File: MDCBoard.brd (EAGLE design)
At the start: 43.9 x 32.6 mm, 200 parts, among them J1 JUMPER-SOLDER, J10 MICROSD-SOCKET, J11 USB-C-RECEPTACLE-KOREANHRO, J2 JUMPER-SOLDER, J3 JUMPER-SOLDER, J4 JUMPER-SOLDER, J5 JST-SM02B-SRSS-TB, J6 JUMPER-SOLDER, J7 JUMPER-SOLDER, J8 JUMPER-SOLDER, Q1 PMOS-NEXPERIA-SOT1220, Q2 PMOS-NEXPERIA-SOT1220, Q3 PMOS-NEXPERIA-SOT1220, Q4 DIODESINC-DMG2305UX, Q5 DIODESINC-DMG2305UX, Q6 DIODESINC-DMG2305UX, Q7 DIODESINC-DMG2305UX, Q8 DIODESINC-DMG2305UX, U1 TI-TPS2116, U10 TI-TPS22919DCK, U11 TI-TPS22919DCK, U12 TI-TPS22919DCK, U13 TI-TPS22919DCK, U14 TI-MSP430FR2422IRHL, U16 TI-TXB0102, U17 PANASONIC-EKMB110711X, U18 LATTICE-ICE40HX4K-BG121, U19 WINBOND-W25Q40EW, U2 DIODESINC-AP7350, U20 NEXPERIA-74LVC1G98-OR-INV-INP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, U21 NEXPERIA-74LVC1G98-BUFFER, U22 ON-AR0330CS1C12SPKA0, U23 ALLIANCE-AS4C8M16MSA-6BIN, U24 STM-STM32F730, U25 DIODESINC-DT1446-04V-7, U26 NEXPERIA-74LVC1G98-INVERTER, U3 NEXPERIA-74LVC1G98-NOR, U4 MICROCHIP-MCP7383X, U5 NEXPERIA-74LVC1G98-INVERTER, U6 EATON-STN101, U7 TI-TPS62A01, U8 TI-TPS62A01, U9 TI-TPS62A01, X1 EPSON-FC-135, X2 SITIME-SIT8021, X3 SITIME-SIT8021

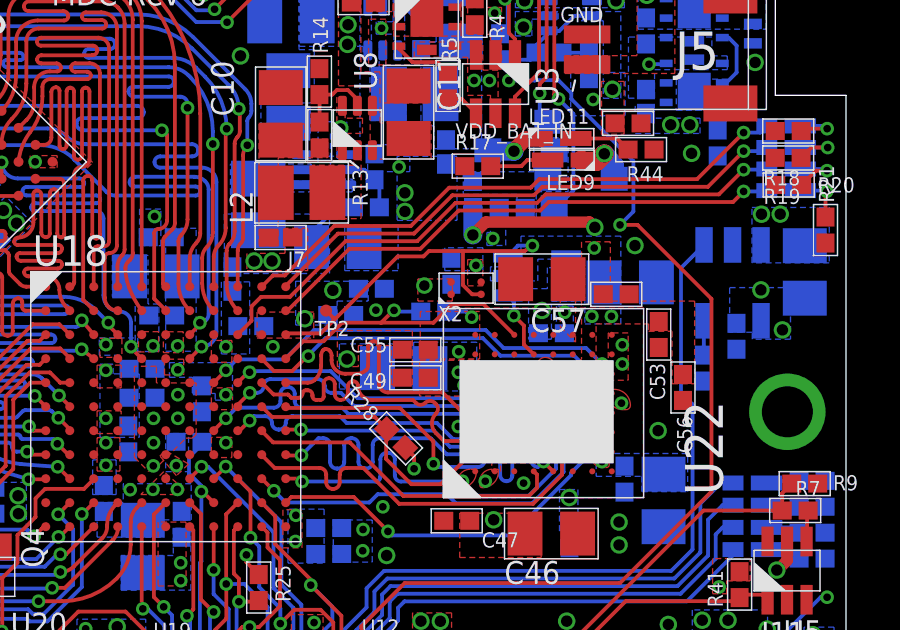
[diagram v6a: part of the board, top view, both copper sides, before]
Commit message: Move components further from lens mount ring
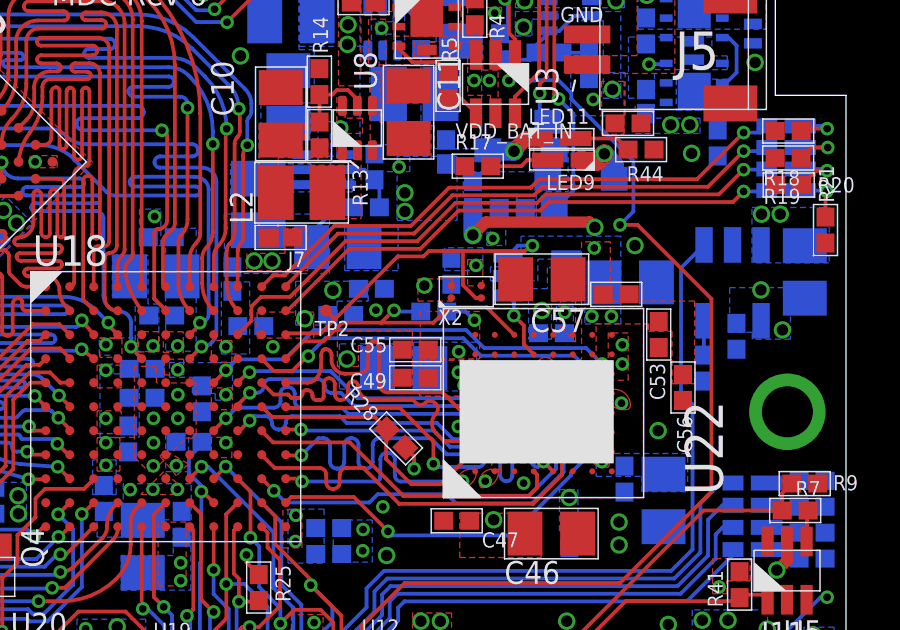
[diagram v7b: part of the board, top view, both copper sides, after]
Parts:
- moved X2 0.12 mm to (31.2, 21.4)
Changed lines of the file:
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@@
 <attribute name="PN" value="GRM155R61H104KE19D" x="37.613171875" y="19.968" size="1.778" layer="27" rot="R270" display="off"/>
 </element>
-<element name="X2" library="EagleLibrary" package="SITIME-SIT8021" value="SITIME-SIT8021" x="31.1912" y="21.513078125" smashed="yes" rot="R90" grouprefs="_ICE_IMG_CLK">
-<attribute name="MFG" value="SiTime" x="31.1912" y="21.513078125" size="1.778" layer="27" rot="R90" display="off"/>
-<attribute name="NAME" x="31.07961875" y="20.914496875" size="0.508" layer="25" font="vector" rot="R180"/>
-<attribute name="PN" value="SIT8021AI-J4-18S-16.000000E" x="31.1912" y="21.513078125" size="1.778" layer="27" rot="R90" display="off"/>
+<element name="X2" library="EagleLibrary" package="SITIME-SIT8021" value="SITIME-SIT8021" x="31.196278125" y="21.393696875" smashed="yes" rot="R90" grouprefs="_ICE_IMG_CLK">
+<attribute name="MFG" value="SiTime" x="31.196278125" y="21.393696875" size="1.778" layer="27" rot="R90" display="off"/>
+<attribute name="NAME" x="31.084696875" y="20.795115625" size="0.508" layer="25" font="vector" rot="R180"/>
+<attribute name="PN" value="SIT8021AI-J4-18S-16.000000E" x="31.196278125" y="21.393696875" size="1.778" layer="27" rot="R90" display="off"/>
 </element>
 <element name="J10" library="EagleLibrary" package="MOLEX-1051620001" value="MICROSD-SOCKET" x="8.78433125" y="8.73151875" smashed="yes" rot="MR180">
@@
 <wire x1="26.5237" y1="20.765559375" x2="26.775790625" y2="20.51346875" width="0.127" layer="1"/>
 <wire x1="26.775790625" y1="20.51346875" x2="26.775790625" y2="20.43620625" width="0.127" layer="1"/>
-<wire x1="31.6912" y1="21.308078125" x2="31.391840625" y2="21.308078125" width="0.127" layer="1"/>
-<wire x1="31.391840625" y1="21.308078125" x2="31.087059375" y2="21.612859375" width="0.127" layer="1"/>
+<wire x1="31.696278125" y1="21.188696875" x2="31.511221875" y2="21.188696875" width="0.127" layer="1"/>
+<wire x1="31.511221875" y1="21.188696875" x2="31.087059375" y2="21.612859375" width="0.127" layer="1"/>
 <via x="33.401" y="22.931121875" extent="1-16" drill="0.254"/>
 <wire x1="33.1409875" y1="22.75078125" x2="33.401" y2="22.931121875" width="0.127" layer="1"/>
@@
 <wire x1="25.9333" y1="19.24781875" x2="25.9333" y2="19.27609375" width="0.127" layer="16"/>
 <wire x1="26.502228125" y1="19.845021875" x2="25.9333" y2="19.27609375" width="0.127" layer="16"/>
-<wire x1="26.502228125" y1="19.845021875" x2="31.75" y2="19.845021875" width="0.127" layer="16"/>
+<wire x1="26.502228125" y1="19.845021875" x2="31.097221875" y2="19.845021875" width="0.127" layer="16"/>
 <wire x1="35.72246875" y1="18.332240625" x2="35.72245625" y2="18.33225625" width="0.127" layer="1"/>
 <wire x1="35.72245625" y1="18.33225625" x2="35.3972" y2="18.007" width="0.127" layer="1"/>
-<wire x1="31.75" y1="19.845021875" x2="32.333140625" y2="19.26188125" width="0.127" layer="16"/>
+<wire x1="31.097221875" y1="19.845021875" x2="31.6803625" y2="19.26188125" width="0.127" layer="16"/>
 <wire x1="34.792828125" y1="19.26188125" x2="35.72246875" y2="18.332240625" width="0.127" layer="16"/>
-<wire x1="32.333140625" y1="19.26188125" x2="34.792828125" y2="19.26188125" width="0.127" layer="16"/>
+<wire x1="31.6803625" y1="19.26188125" x2="34.792828125" y2="19.26188125" width="0.127" layer="16"/>
 </signal>
 <signal name="IMG_D2">
@@
 <wire x1="23.1836" y1="18.7672" x2="22.7794" y2="18.363" width="0.127" layer="1"/>
 <wire x1="25.14038125" y1="19.1389" x2="26.11934375" y2="20.1178625" width="0.127" layer="16"/>
-<wire x1="26.11934375" y1="20.1178625" x2="31.84144375" y2="20.1178625" width="0.127" layer="16"/>
+<wire x1="26.11934375" y1="20.1178625" x2="31.19628125" y2="20.1178625" width="0.127" layer="16"/>
 <wire x1="35.722471875" y1="18.985021875" x2="35.722471875" y2="18.982271875" width="0.127" layer="1"/>
 <wire x1="35.722471875" y1="18.982271875" x2="35.3972" y2="18.657" width="0.127" layer="1"/>
 <wire x1="23.1836" y1="18.7742" x2="23.5483" y2="19.1389" width="0.127" layer="16"/>
 <wire x1="23.5483" y1="19.1389" x2="25.14038125" y2="19.1389" width="0.127" layer="16"/>
-<wire x1="31.84144375" y1="20.1178625" x2="32.441946875" y2="19.517359375" width="0.127" layer="16"/>
+<wire x1="31.19628125" y1="20.1178625" x2="31.796784375" y2="19.517359375" width="0.127" layer="16"/>
 <wire x1="35.190134375" y1="19.517359375" x2="35.722471875" y2="18.985021875" width="0.127" layer="16"/>
-<wire x1="32.441946875" y1="19.517359375" x2="35.190134375" y2="19.517359375" width="0.127" layer="16"/>
+<wire x1="31.796784375" y1="19.517359375" x2="35.190134375" y2="19.517359375" width="0.127" layer="16"/>
 </signal>
 <signal name="VCCPLL0">
@@
 <wire x1="25.1794" y1="19.163" x2="25.75968125" y2="19.74328125" width="0.127" layer="1"/>
 <wire x1="25.75968125" y1="19.74328125" x2="26.44208125" y2="19.74328125" width="0.127" layer="1"/>
-<wire x1="30.103021875" y1="20.36064375" x2="30.722259375" y2="20.97988125" width="0.127" layer="1"/>
-<wire x1="31.77431875" y1="20.97988125" x2="30.722259375" y2="20.97988125" width="0.127" layer="1"/>
+<wire x1="30.103021875" y1="20.36064375" x2="30.61558125" y2="20.873203125" width="0.127" layer="1"/>
+<wire x1="31.880996875" y1="20.873203125" x2="30.61558125" y2="20.873203125" width="0.127" layer="1"/>
 <via x="28.788359375" y="20.77211875" extent="1-16" drill="0.254"/>
 <wire x1="28.7699375" y1="20.77211875" x2="28.788359375" y2="20.77211875" width="0.127" layer="1"/>
@@
 <wire x1="29.679728125" y1="20.732534375" x2="28.82794375" y2="20.732534375" width="0.127" layer="16"/>
 <wire x1="28.82794375" y1="20.732534375" x2="28.788359375" y2="20.77211875" width="0.127" layer="16"/>
-<wire x1="31.77431875" y1="20.97988125" x2="32.7972" y2="19.957" width="0.127" layer="1"/>
+<wire x1="31.880996875" y1="20.873203125" x2="32.7972" y2="19.957" width="0.127" layer="1"/>
 </signal>
 <signal name="IMG_SCLK">
@@
 <via x="4.364740625" y="4.99871875" extent="1-16" drill="0.254"/>
 <via x="4.364740625" y="4.295140625" extent="1-16" drill="0.254"/>
-<via x="31.377640625" y="20.546059375" extent="1-16" drill="0.254"/>
+<via x="31.4706" y="20.444459375" extent="1-16" drill="0.254"/>
 <via x="35.461971875" y="22.852384375" extent="1-16" drill="0.254"/>
 <via x="29.45714375" y="15.494" extent="1-16" drill="0.254"/>
@@
 <wire x1="4.673240625" y1="5.15570625" x2="4.673240625" y2="7.366" width="0.381" layer="15"/>
 <wire x1="4.673240625" y1="7.366" x2="4.673240625" y2="10.563953125" width="0.381" layer="15"/>
-<wire x1="30.544728125" y1="20.732534375" x2="31.191165625" y2="20.732534375" width="0.127" layer="16"/>
-<wire x1="31.191165625" y1="20.732534375" x2="31.377640625" y2="20.546059375" width="0.127" layer="16"/>
+<wire x1="30.544728125" y1="20.732534375" x2="31.16830625" y2="20.732534375" width="0.127" layer="16"/>
+<wire x1="31.16830625" y1="20.732534375" x2="31.4706" y2="20.444459375" width="0.127" layer="16"/>
 <via x="5.76071875" y="7.12978125" extent="1-16" drill="0.381"/>
 <wire x1="4.751525" y1="7.59434375" x2="5.2160875" y2="7.12978125" width="0.635" layer="1"/>
@@
 <wire x1="5.76071875" y1="7.12978125" x2="4.909459375" y2="7.12978125" width="0.381" layer="15"/>
 <wire x1="4.909459375" y1="7.12978125" x2="4.673240625" y2="7.366" width="0.381" layer="15"/>
-<wire x1="30.945840625" y1="19.395440625" x2="30.945840625" y2="20.114259375" width="0.381" layer="15"/>
-<wire x1="30.945840625" y1="20.114259375" x2="31.377640625" y2="20.546059375" width="0.381" layer="15"/>
-<wire x1="31.377640625" y1="20.546059375" x2="31.377640625" y2="20.555646875" width="0.381" layer="15"/>
-<wire x1="31.377640625" y1="20.555646875" x2="32.772146875" y2="21.950153125" width="0.381" layer="15"/>
+<wire x1="30.945840625" y1="19.395440625" x2="30.945840625" y2="19.93391875" width="0.381" layer="15"/>
+<wire x1="30.945840625" y1="19.93391875" x2="31.4706" y2="20.444459375" width="0.381" layer="15"/>
+<wire x1="31.4706" y1="20.444459375" x2="31.45638125" y2="20.6343875" width="0.381" layer="15"/>
+<wire x1="31.45638125" y1="20.6343875" x2="32.772146875" y2="21.950153125" width="0.381" layer="15"/>
 <wire x1="34.156978125" y1="22.852384375" x2="34.402784375" y2="22.852384375" width="0.381" layer="15"/>
 <wire x1="24.98630625" y1="25.654" x2="26.76430625" y2="27.432" width="0.381" layer="15"/>

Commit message: Layout progress
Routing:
- net GND: vias 77 -> 78
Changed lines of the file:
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@@
 <grid distance="10" unitdist="mil" unit="mil" style="lines" multiple="1" display="no" altdistance="0.00254" altunitdist="mm" altunit="mil"/>
 <layers>
-<layer number="1" name="Top" color="4" fill="1" visible="yes" active="yes"/>
+<layer number="1" name="Top" color="4" fill="1" visible="no" active="yes"/>
 <layer number="2" name="Ground" color="16" fill="1" visible="no" active="yes"/>
 <layer number="3" name="Route3" color="17" fill="1" visible="no" active="no"/>
@@
 <layer number="14" name="Route14" color="22" fill="1" visible="no" active="no"/>
 <layer number="15" name="Power" color="42" fill="1" visible="no" active="yes"/>
-<layer number="16" name="Bottom" color="1" fill="1" visible="no" active="yes"/>
+<layer number="16" name="Bottom" color="1" fill="1" visible="yes" active="yes"/>
 <layer number="17" name="Pads" color="2" fill="1" visible="yes" active="yes"/>
 <layer number="18" name="Vias" color="2" fill="1" visible="yes" active="yes"/>
 <layer number="19" name="Unrouted" color="6" fill="1" visible="no" active="yes"/>
 <layer number="20" name="Dimension" color="24" fill="1" visible="yes" active="yes"/>
-<layer number="21" name="tPlace" color="7" fill="1" visible="yes" active="yes"/>
-<layer number="22" name="bPlace" color="7" fill="1" visible="no" active="yes"/>
-<layer number="23" name="tOrigins" color="15" fill="1" visible="yes" active="yes"/>
-<layer number="24" name="bOrigins" color="15" fill="1" visible="no" active="yes"/>
-<layer number="25" name="tNames" color="7" fill="1" visible="yes" active="yes"/>
-<layer number="26" name="bNames" color="7" fill="1" visible="no" active="yes"/>
-<layer number="27" name="tValues" color="7" fill="1" visible="yes" active="yes"/>
-<layer number="28" name="bValues" color="7" fill="1" visible="no" active="yes"/>
-<layer number="29" name="tStop" color="7" fill="3" visible="yes" active="yes"/>
-<layer number="30" name="bStop" color="7" fill="6" visible="no" active="yes"/>
-<layer number="31" name="tCream" color="7" fill="4" visible="yes" active="yes"/>
-<layer number="32" name="bCream" color="7" fill="5" visible="no" active="yes"/>
-<layer number="33" name="tFinish" color="6" fill="3" visible="yes" active="yes"/>
-<layer number="34" name="bFinish" color="6" fill="6" visible="no" active="yes"/>
-<layer number="35" name="tGlue" color="7" fill="4" visible="yes" active="yes"/>
-<layer number="36" name="bGlue" color="7" fill="5" visible="no" active="yes"/>
-<layer number="37" name="tTest" color="7" fill="1" visible="yes" active="yes"/>
-<layer number="38" name="bTest" color="7" fill="1" visible="no" active="yes"/>
-<layer number="39" name="tKeepout" color="4" fill="11" visible="yes" active="yes"/>
-<layer number="40" name="bKeepout" color="1" fill="11" visible="no" active="yes"/>
-<layer number="41" name="tRestrict" color="4" fill="10" visible="yes" active="yes"/>
-<layer number="42" name="bRestrict" color="1" fill="10" visible="no" active="yes"/>
+<layer number="21" name="tPlace" color="7" fill="1" visible="no" active="yes"/>
+<layer number="22" name="bPlace" color="7" fill="1" visible="yes" active="yes"/>
+<layer number="23" name="tOrigins" color="15" fill="1" visible="no" active="yes"/>
+<layer number="24" name="bOrigins" color="15" fill="1" visible="yes" active="yes"/>
+<layer number="25" name="tNames" color="7" fill="1" visible="no" active="yes"/>
+<layer number="26" name="bNames" color="7" fill="1" visible="yes" active="yes"/>
+<layer number="27" name="tValues" color="7" fill="1" visible="no" active="yes"/>
+<layer number="28" name="bValues" color="7" fill="1" visible="yes" active="yes"/>
+<layer number="29" name="tStop" color="7" fill="3" visible="no" active="yes"/>
+<layer number="30" name="bStop" color="7" fill="6" visible="yes" active="yes"/>
+<layer number="31" name="tCream" color="7" fill="4" visible="no" active="yes"/>
+<layer number="32" name="bCream" color="7" fill="5" visible="yes" active="yes"/>
+<layer number="33" name="tFinish" color="6" fill="3" visible="no" active="yes"/>
+<layer number="34" name="bFinish" color="6" fill="6" visible="yes" active="yes"/>
+<layer number="35" name="tGlue" color="7" fill="4" visible="no" active="yes"/>
+<layer number="36" name="bGlue" color="7" fill="5" visible="yes" active="yes"/>
+<layer number="37" name="tTest" color="7" fill="1" visible="no" active="yes"/>
+<layer number="38" name="bTest" color="7" fill="1" visible="yes" active="yes"/>
+<layer number="39" name="tKeepout" color="4" fill="11" visible="no" active="yes"/>
+<layer number="40" name="bKeepout" color="1" fill="11" visible="yes" active="yes"/>
+<layer number="41" name="tRestrict" color="4" fill="10" visible="no" active="yes"/>
+<layer number="42" name="bRestrict" color="1" fill="10" visible="yes" active="yes"/>
 <layer number="43" name="vRestrict" color="2" fill="10" visible="no" active="yes"/>
 <layer number="44" name="Drills" color="7" fill="1" visible="no" active="yes"/>
@@
 <polygon width="0.127" layer="16" thermals="no">
 <vertex x="27.146" y="23.622"/>
-<vertex x="28.924" y="23.622"/>
-<vertex x="28.924" y="22.098"/>
+<vertex x="29.117040625" y="23.622"/>
+<vertex x="29.117040625" y="22.098"/>
 <vertex x="27.146" y="22.098"/>
 </polygon>
@@
 <vertex x="32.512" y="24.384"/>
 </polygon>
+<via x="28.84931875" y="22.33168125" extent="1-16" drill="0.381"/>
 </signal>
 <signal name="ICE_IMG_CLK16MHZ">
@@
 <via x="33.401" y="22.931121875" extent="1-16" drill="0.254"/>
 <wire x1="33.1409875" y1="22.75078125" x2="33.401" y2="22.931121875" width="0.127" layer="1"/>
-<wire x1="28.910028125" y1="22.57044375" x2="29.77233125" y2="22.57044375" width="0.127" layer="1"/>
-<wire x1="29.77233125" y1="22.57044375" x2="29.95266875" y2="22.75078125" width="0.127" layer="1"/>
-<wire x1="26.775790625" y1="20.43620625" x2="28.910028125" y2="22.57044375" width="0.127" layer="1"/>
-<wire x1="29.95266875" y1="22.75078125" x2="31.087059375" y2="22.75078125" width="0.127" layer="1"/>
+<wire x1="27.558746875" y1="21.2191625" x2="28.743628125" y2="21.2191625" width="0.127" layer="1"/>
+<wire x1="28.743628125" y1="21.2191625" x2="30.275246875" y2="22.75078125" width="0.127" layer="1"/>
+<wire x1="26.775790625" y1="20.43620625" x2="27.558746875" y2="21.2191625" width="0.127" layer="1"/>
+<wire x1="30.275246875" y1="22.75078125" x2="31.087059375" y2="22.75078125" width="0.127" layer="1"/>
 <wire x1="31.087059375" y1="22.75078125" x2="33.1409875" y2="22.75078125" width="0.127" layer="1"/>
 <wire x1="31.087059375" y1="21.612859375" x2="31.087059375" y2="22.75078125" width="0.127" layer="1"/>
